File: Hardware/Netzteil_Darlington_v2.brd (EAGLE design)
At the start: 152 x 120 mm, 149 parts, among them IC1 7815TV, IC11 OPA2197, IC12 MAX4080F, IC13 OPA2197, IC15 LD33V, IC17 7815TV, IC18 7812TV, IC2 OPA2197, IC4 LM358ADR, IC5 OPA2197, IC6 TPS5430, IC9 LM334, T1 IRLL110TRPBF, T3 BD139, T4 2N5401, T5 TIP3055, T6 TIP3055, T7 BD139, T8 BC847ALT1G, T9 BUJ303B,127

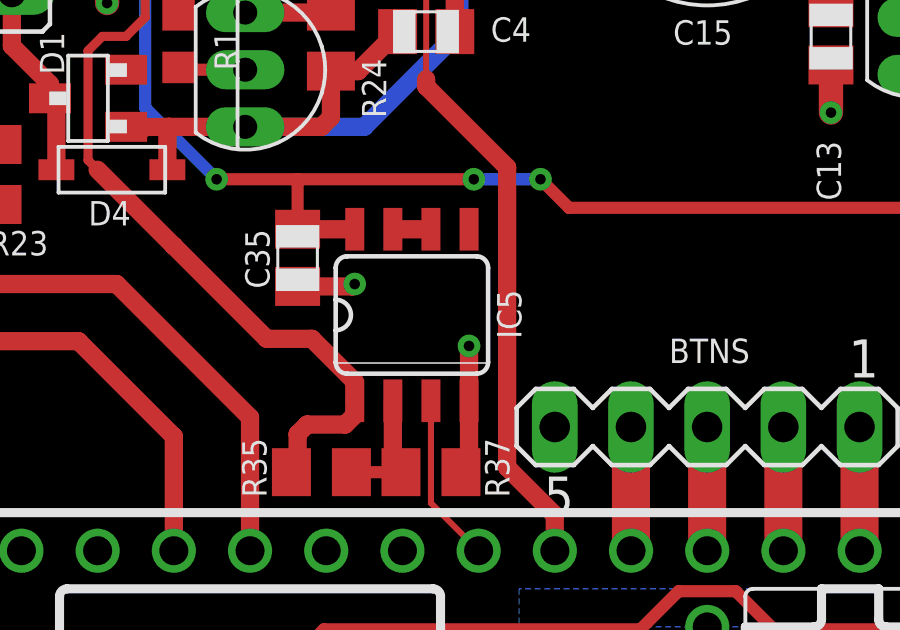
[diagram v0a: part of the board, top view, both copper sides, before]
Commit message: Add files via upload
fix second, floating, unused ISET opamp (IC5B)
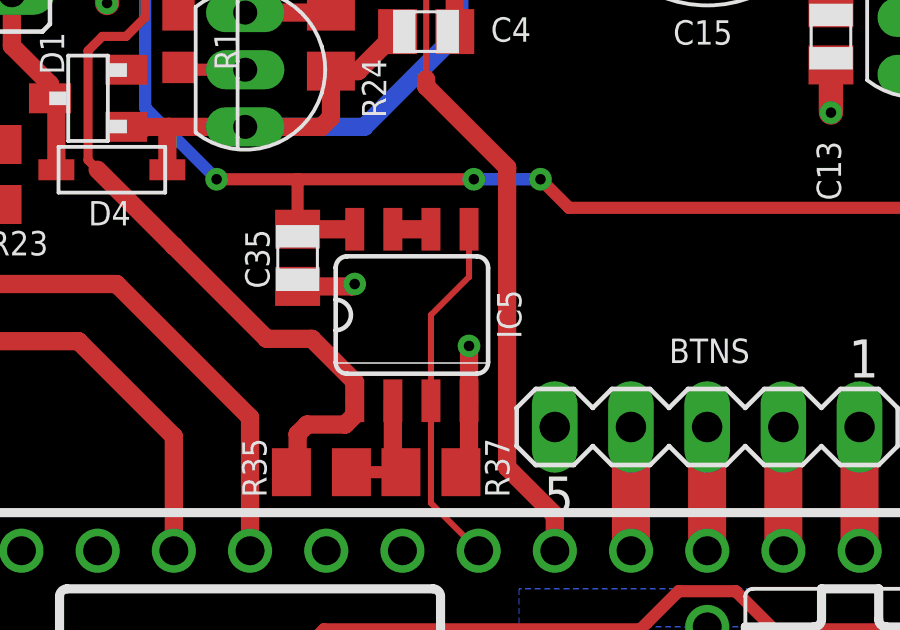
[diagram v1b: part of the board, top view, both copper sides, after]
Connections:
- net ISET: now also IC5.5
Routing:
- net ISET: track 5.66 -> 11.9 mm
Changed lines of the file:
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@@
 <setting verticaltext="up"/>
 </settings>
-<grid distance="0.15875" unitdist="mm" unit="mm" style="lines" multiple="1" display="yes" altdistance="5" altunitdist="mil" altunit="mil"/>
+<grid distance="0.635" unitdist="mm" unit="mm" style="lines" multiple="1" display="no" altdistance="5" altunitdist="mil" altunit="mil"/>
 <layers>
 <layer number="1" name="Top" color="4" fill="1" visible="yes" active="yes"/>
@@
 <wire x1="80.3275" y1="50.165" x2="80.3275" y2="46.754659375" width="0.2032" layer="1"/>
 <wire x1="80.3275" y1="46.754659375" x2="81.9171625" y2="45.164996875" width="0.2032" layer="1"/>
+<contactref element="IC5" pad="5"/>
+<wire x1="80.3275" y1="50.165" x2="80.3275" y2="53.0225" width="0.2032" layer="1"/>
+<wire x1="81.5975" y1="54.2925" x2="81.5975" y2="55.88" width="0.2032" layer="1"/>
+<wire x1="80.3275" y1="53.0225" x2="81.5975" y2="54.2925" width="0.2032" layer="1"/>
 </signal>
 <signal name="N$40">

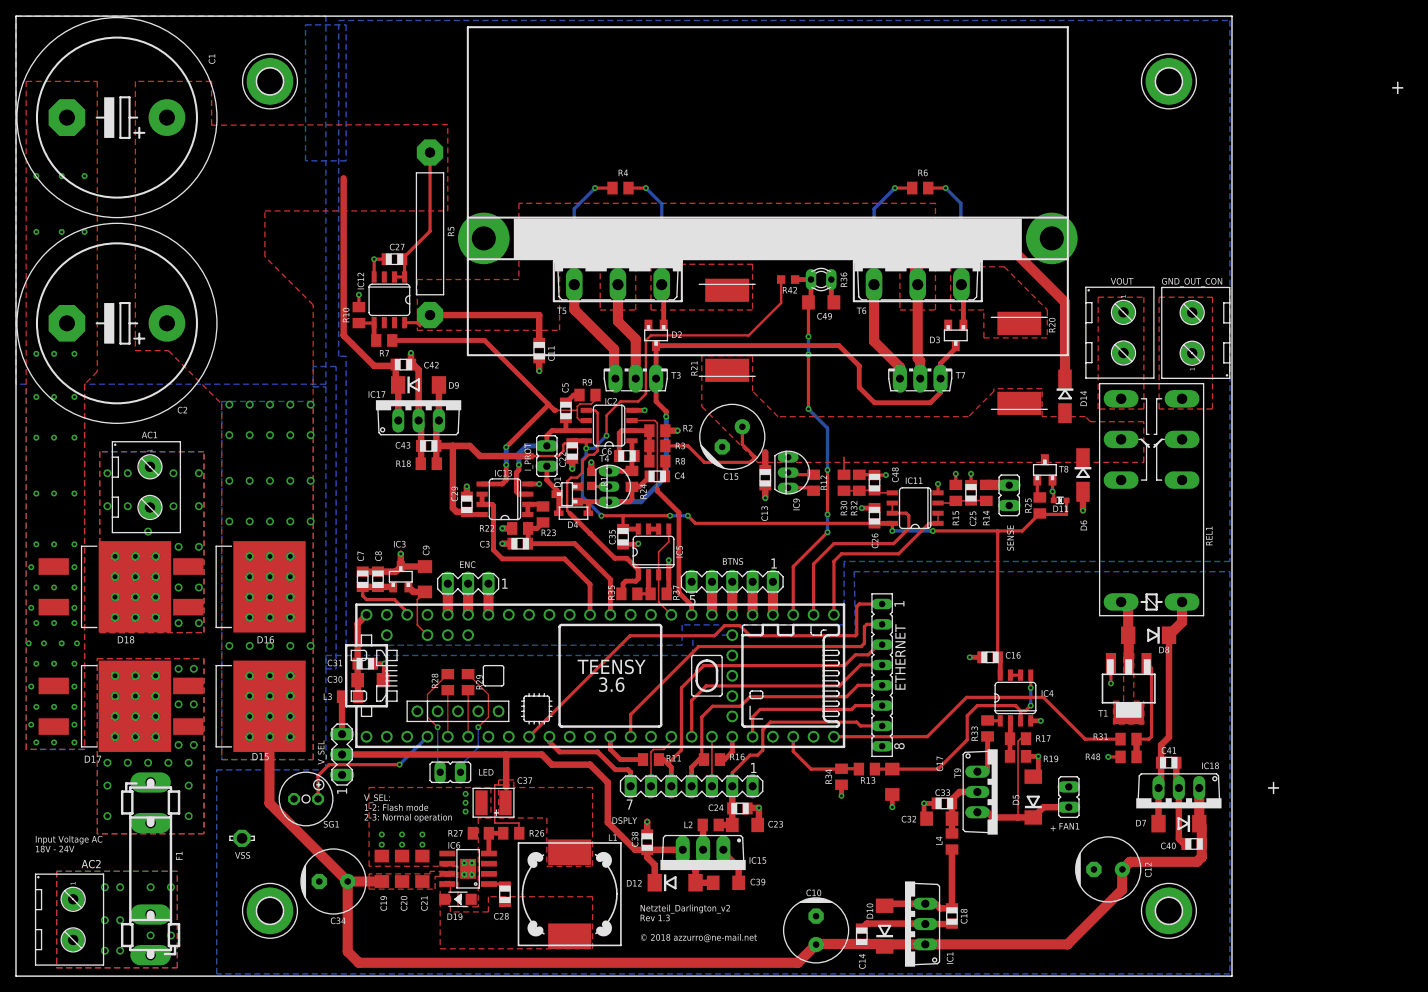
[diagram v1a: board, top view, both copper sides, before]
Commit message: update to rev 1.6
fix several bugs and issues
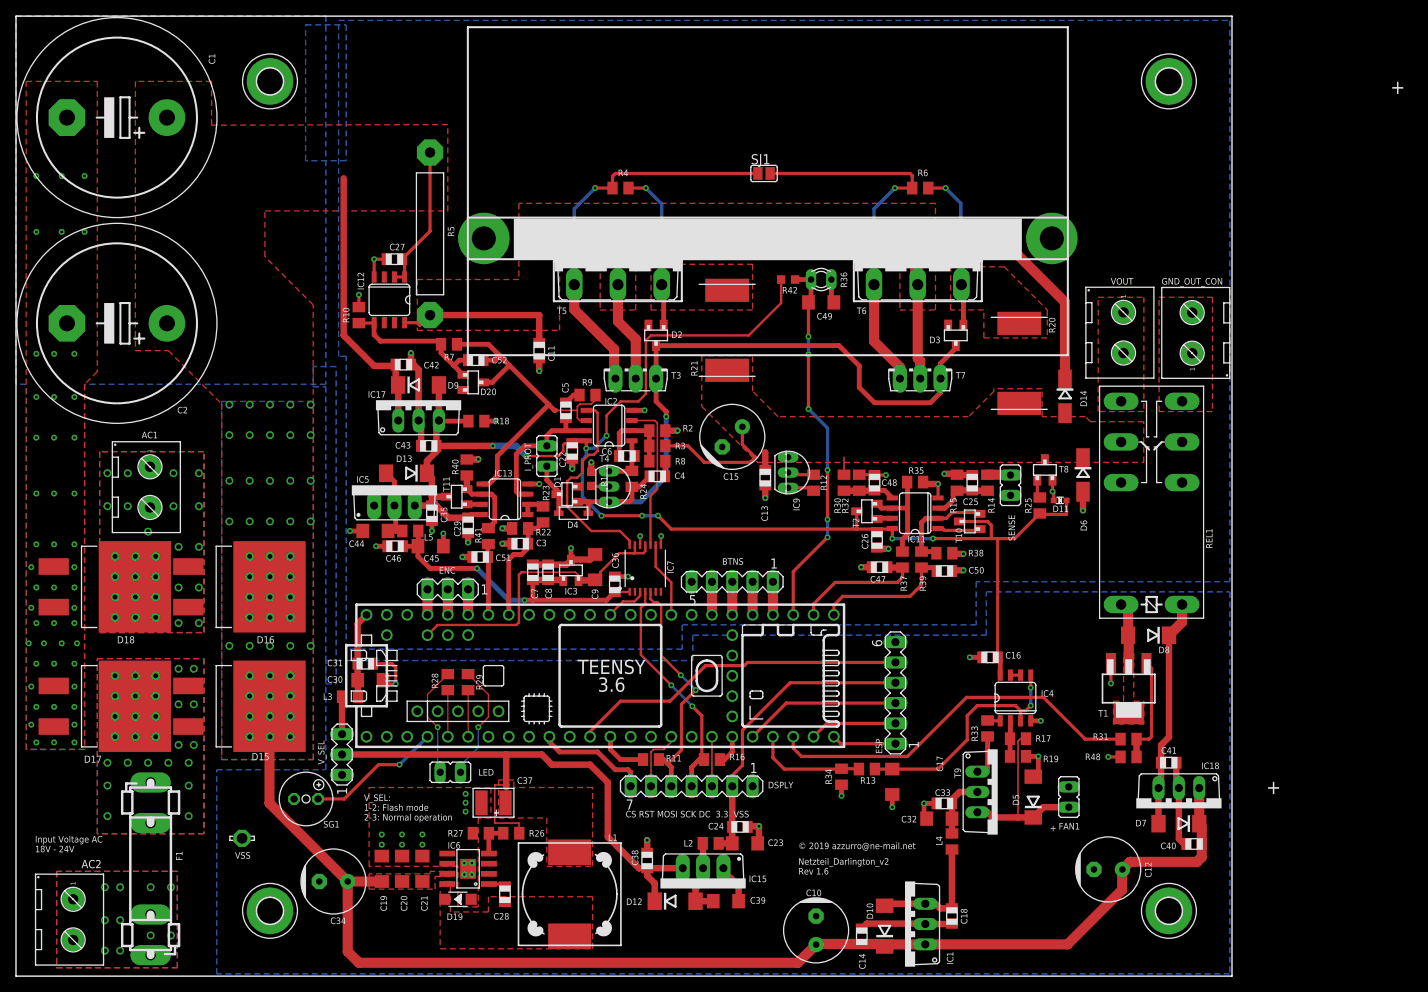
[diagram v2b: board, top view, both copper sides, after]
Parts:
- removed ETHERNET: (no value), con-lsta:FE08
- added C36, C46, C52: 100n, goujine:0805
- added C44, C45: 10µ / C3216X7R1E106M160AB, goujine:1206
- added C47, C50, C51: 10n, goujine:0805
- added D13: 1N4007, diode:DO214AA
- added D20: BAT54FILMY, neumluc:SOT23
- added ESP: (no value), con-lstb:MA06-1
- added IC7: MCP4922, neumluc:TSSOP14
- added L5: MPZ2012S601AT000, neumluc:C0805K
- added R38, R40: 4.7k, neumluc:C0805K
- added R39, R41: 100R, neumluc:C0805K
- added SJ1: (no value), jumper:SJ
- added T10, T11, T2: BC847ALT1G, neumluc:SOT23-BEC
- IC5: value OPA2197 -> LD33V; device goujine:SOP8 -> neumluc:TO220V
- R14, R23, R30: value 81k 0.1% low PPM -> 90.9k 0.1% RN73C2A90K9BTDF
- R15, R22, R32: value 9k1 0.1% low PPM -> 10.1k 0.1% RN732ATTD1012B25
- R18: value 2k5 -> 2k2
- R2: value 1.27k 0.1% low PPM -> 2.4k 0.1% PCF0805-13-2K4BT1
- R3: value 20k5 0.1% low PPM -> 12k 0.1% ERA-6ARW123V
- R35: value 20k 0.1% low PPM -> 4.7k
- R37: value 28.02k 0.1% low PPM -> 100R
- moved R35 38.4 mm to (112.4, 61.8)
- moved IC5 32.9 mm to (47.3, 58.8)
- moved R37 30.8 mm to (110.8, 52.1), turned to 270 degrees
- moved C35 24.1 mm to (52.0, 57.9)
- moved C9 21.3 mm to (72.4, 51.1)
- moved C7 21.3 mm to (64.6, 50.5)
- moved C8 21.3 mm to (66.5, 50.5)
- moved IC3 21.3 mm to (69.4, 50.7)
- moved R7 8.11 mm to (54.1, 79.0)
- moved R18 7.98 mm to (57.5, 69.4), turned to 0 degrees
- moved C26 3.03 mm to (107.6, 54.5), turned to 270 degrees
- moved ENC 2.64 mm to (54.0, 48.3)
- moved C29 2.63 mm to (56.5, 56.4), turned to 270 degrees
- moved C38 2.30 mm to (78.9, 14.4)
- moved C39 2.30 mm to (88.7, 9.36)
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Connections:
- removed net +3.3V_LP: C7.1, C8.1, IC3.1, U$33.3V3_LO
- removed net ETH_CS: ETHERNET.6, U$33.28
- removed net ETH_INT: ETHERNET.4, U$33.25
- removed net ETH_RST: ETHERNET.1, U$33.7
- removed net ISET_AMP: IC2.5, IC5.1, R35.1
- removed net RESET: U$33.RESET
- new net +3.3V_A: C36.2, C45.1, C46.1, C7.1, C8.1, IC3.1, IC7.1, L5.2
- new net DAC_CS: IC7.3, U$33.14/A0
- new net DAC_SHDN: IC7.9, U$33.A22/DAC1
- new net ESP-IO: ESP.5, U$33.10/CS
- new net ESP-RST: ESP.3, U$33.28
- new net ESP-RX: ESP.2, U$33.31/A12
- new net ESP-TX: ESP.1, U$33.32/A13
- new net N$41: IC11.6, R35.1, R37.1, T2.E
- new net N$42: IC11.1, T10.B
- new net N$43: IC11.2, R38.1, R39.1, T10.E
- new net N$44: IC13.7, T11.B
- new net N$45: IC13.6, R40.1, R41.1, T11.E
- net +15V: now also D13.C, IC5.3, T10.C, T11.C, T2.C; no longer IC5.8
- net +3.3V: now also ESP.4; no longer ETHERNET.7
- net ADC_CH0: now also C51.1, R41.2, U$33.20/A6; no longer IC13.6, IC13.7, U$33.15/A1
- net ADC_CH1: now also C50.1, R39.2; no longer IC11.1, IC11.2
- net ADC_CH2: now also C47.1, R37.2; no longer IC11.6, IC11.7
- net ADC_CH3: now also U$33.19/A5/SCL; no longer U$33.14/A0
- net AGND: now also C36.1, C44.1, C45.2, C46.2, C47.2, C50.2, C51.2, IC5.1, IC7.12, IC7.8, R35.2, R38.2, R40.2; no longer IC5.4, R37.2
- net AREF2048: now also IC7.11, IC7.13
- net CRNT_READ: now also C52.1, D20.3
- net ENC_A: now also U$33.21/A7; no longer U$33.20/A6
- net ENC_B: now also U$33.22/A8; no longer U$33.21/A7
- net ENC_BTN: now also U$33.23/A9; no longer U$33.22/A8
- net FAN-OUT: now also U$33.29; no longer U$33.30
- net ISET: now also IC2.5, IC7.14; no longer IC5.3, IC5.5, U$33.A22/DAC1
- net MISO: no longer ETHERNET.2
- net MOSI: now also IC7.5; no longer ETHERNET.3
- net N$15: now also SJ1.1
- net N$39: now also C44.2, D13.A, IC5.2, L5.1; no longer IC5.6, IC5.7
- net N$40: now also IC11.7, T2.B; no longer IC5.2, R35.2, R37.1
- net N$5: now also SJ1.2
- net N$7: now also C52.2, D20.1
- net REL-OUT: now also U$33.30; no longer U$33.32/A13
- net SCK: now also IC7.4; no longer ETHERNET.5
- net VSET: now also IC7.10; no longer U$33.21/DAC0
- net VSS: now also ESP.6; no longer ETHERNET.8
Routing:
- net ETH_RST: track 54.1 -> 0.00 mm
- net ESP-IO: track 0.00 -> 42.4 mm
- net +3.3V_A: track 0.00 -> 40.8 mm, vias 0 -> 2
- net MISO: track 40.1 -> 0.00 mm
- net ISET_AMP: track 32.8 -> 0.00 mm
- net ETH_INT: track 30.2 -> 0.00 mm
- net AREF2048: track 8.65 -> 38.4 mm
- net N$15: track 29.2 -> 49.0 mm
- net ESP-RST: track 0.00 -> 19.6 mm
- net N$5: track 28.4 -> 47.8 mm
- net ETH_CS: track 19.2 -> 0.00 mm
- net ADC_CH0: track 26.0 -> 8.91 mm
- net N$7: track 4.26 -> 19.3 mm
- net ISET: track 11.9 -> 25.8 mm
- net N$43: track 0.00 -> 13.4 mm
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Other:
- board text added: "CS RST MOSI SCK DC 3.3 VSS"
- board text added: "Netzteil_Darlington_v2 Rev 1.6"
- board text added: "© 2019 azzurro@ne-mail.net"
- board text removed: "Netzteil_Darlington_v2 Rev 1.3 © 2018 azzurro@ne-mail.net"
